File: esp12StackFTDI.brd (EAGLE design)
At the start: 31.5 x 30 mm, 35 parts, among them J02 470, J04 470, J05 470, J12 470, J13 470

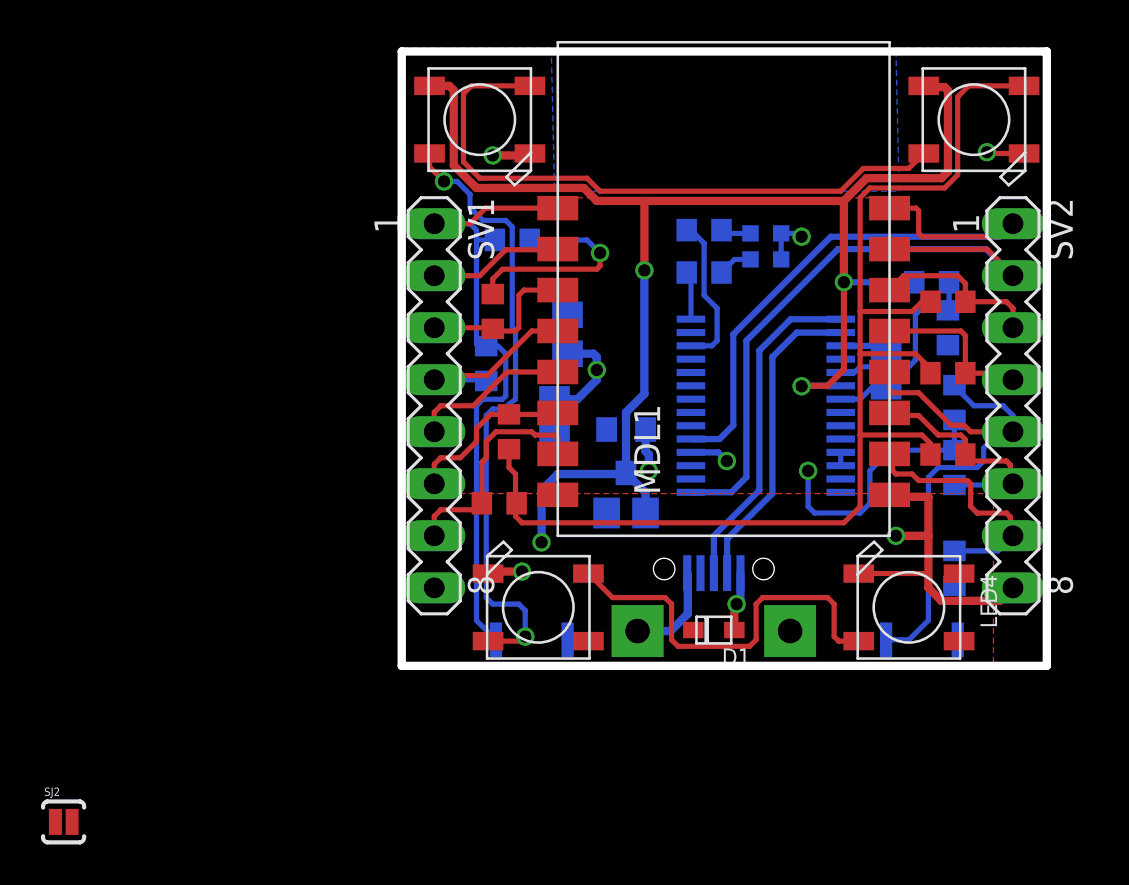
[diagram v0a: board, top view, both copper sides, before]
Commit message: initial test with solder jumpers
added solder jumpers instead of 0603 positions
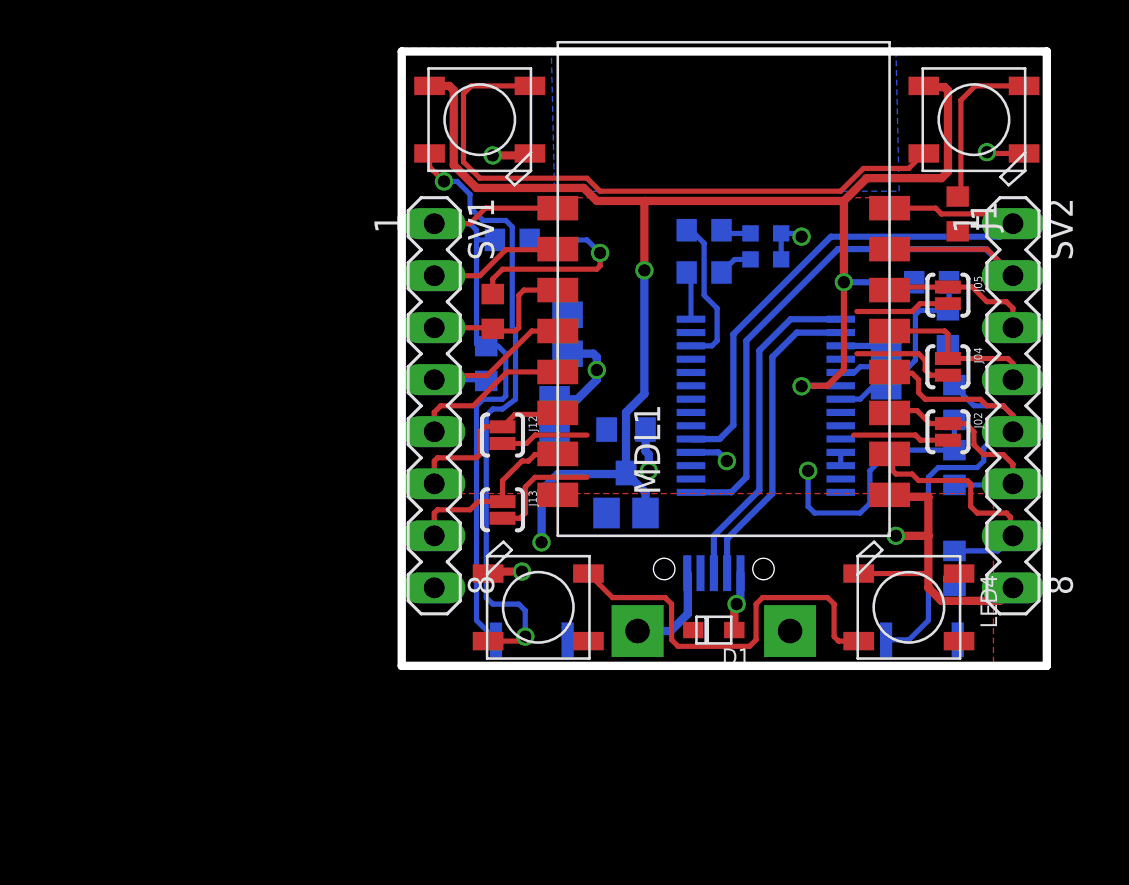
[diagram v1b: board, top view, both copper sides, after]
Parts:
- removed SJ2: SOLDERJUMPERNC2, SparkFun:SJ_2S-NOTRACE
- added J1: 470, eagle-ltspice:R0603
- J02, J04, J05, J12, J13: value 470 -> SOLDERJUMPERNC2; device eagle-ltspice:R0603 -> SparkFun:SJ_2S-NOTRACE
- moved J13 3.82 mm to (4.92, 7.62), turned to 270 degrees
- moved J12 3.34 mm to (4.92, 11.3), turned to 270 degrees
- moved J02 1.11 mm to (26.7, 11.4), turned to 270 degrees
- moved J04 0.32 mm to (26.7, 14.6), turned to 270 degrees
- moved J05 0.32 mm to (26.7, 18.1), turned to 270 degrees
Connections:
- new net N$2: J1.1, LED1.4-DIN
- net DIN1: now also J02.2, J04.2, J05.2, J1.2, J12.2, J13.2; no longer J02.1, J04.1, J05.1, J12.1, J13.1, LED1.4-DIN, SJ2.2
- net GPIO12: now also J12.1; no longer J13.2
- net GPIO13: now also J13.1; no longer J12.2
- net GPIO2: now also J02.1; no longer J02.2, SJ2.1
- net GPIO4: now also J04.1; no longer J04.2
- net GPIO5: now also J05.1; no longer J05.2
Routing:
- net DIN1: track 60.1 -> 24.5 mm
- net N$2: track 0.00 -> 8.15 mm
- net GPIO13: track 12.6 -> 9.13 mm
- net TXD: track 30.5 -> 29.3 mm
- net GPIO5: track 8.47 -> 7.48 mm

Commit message: optimizing solder jumpers
different placement for the solder jumpers
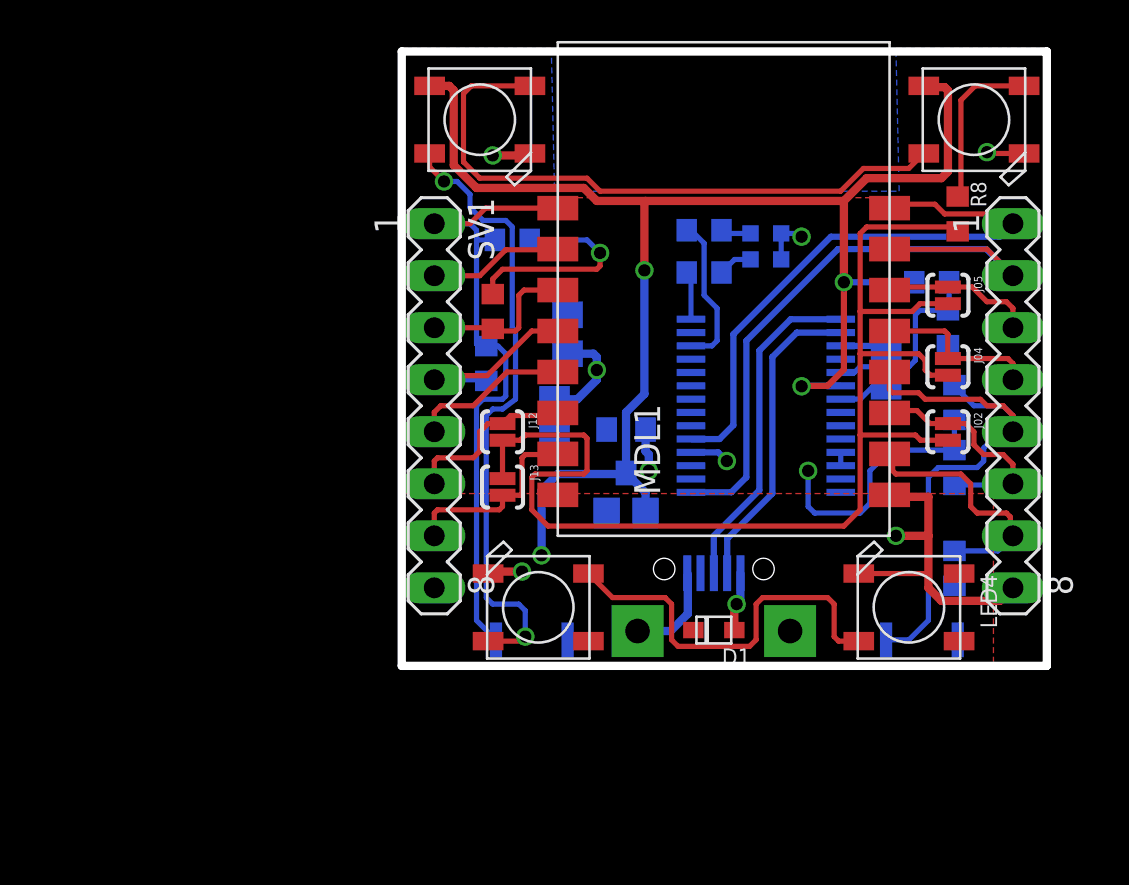
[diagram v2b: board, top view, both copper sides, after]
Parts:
- moved J13 1.11 mm to (4.92, 8.73), turned to 90 degrees
- moved J12 0.16 mm to (4.92, 11.4)
- renumbered J1 to R8
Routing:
- net DIN1: track 24.5 -> 61.2 mm
- net GPIO13: track 9.13 -> 9.88 mm
- net 5V: track 74.8 -> 75.4 mm

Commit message: some major updates
* working ft232rl layout
* replaced the DIN resistors for the WS2112 with solder jumpers
* sensors breakout board
* fixed a bug (missing trace) in the rgbwwpw board
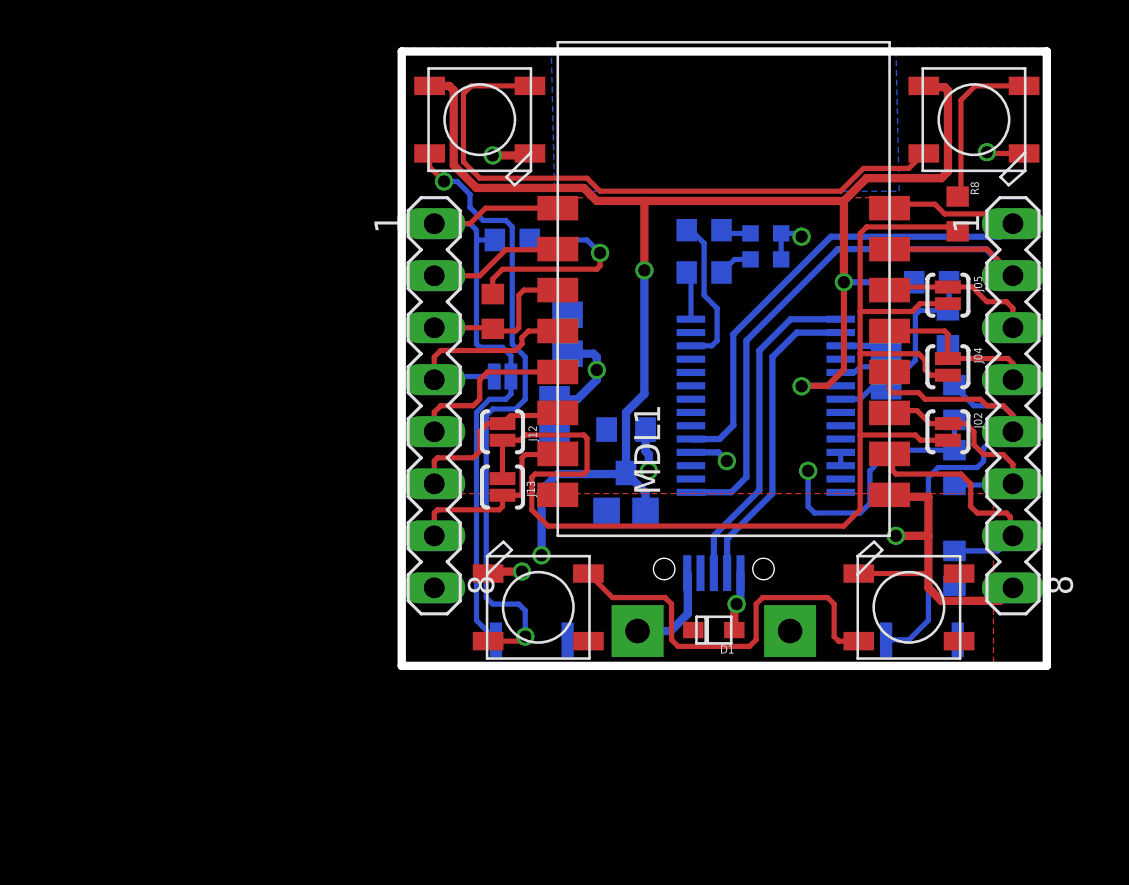
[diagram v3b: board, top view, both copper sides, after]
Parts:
- removed J_REST: 10k, eagle-ltspice:R0603
- added J01: SOLDERJUMPERNC2, SparkFun:SJ_2S-NOTRACE
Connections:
- net GPIO16: now also J01.1; no longer J_REST.1
- net REST: now also J01.2; no longer J_REST.2
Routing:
- net GPIO16: track 10.3 -> 11.2 mm
- net DOUT2DIN3: track 30.7 -> 31.4 mm
- net GPIO14: track 8.08 -> 8.64 mm
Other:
- board text removed: "G12"
